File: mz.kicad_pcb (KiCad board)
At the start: 2 copper layers, 79 x 68 mm, 32 parts, among them CON1 USB-MINI-B, P1 JTAG, P2 CONN_20, P3 CONN_20, P4 CONN_20, P5 CONN_20, P6 CONN_20, P7 CONN_20, SW1 RESET, U1 NCP1117ST50T3G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

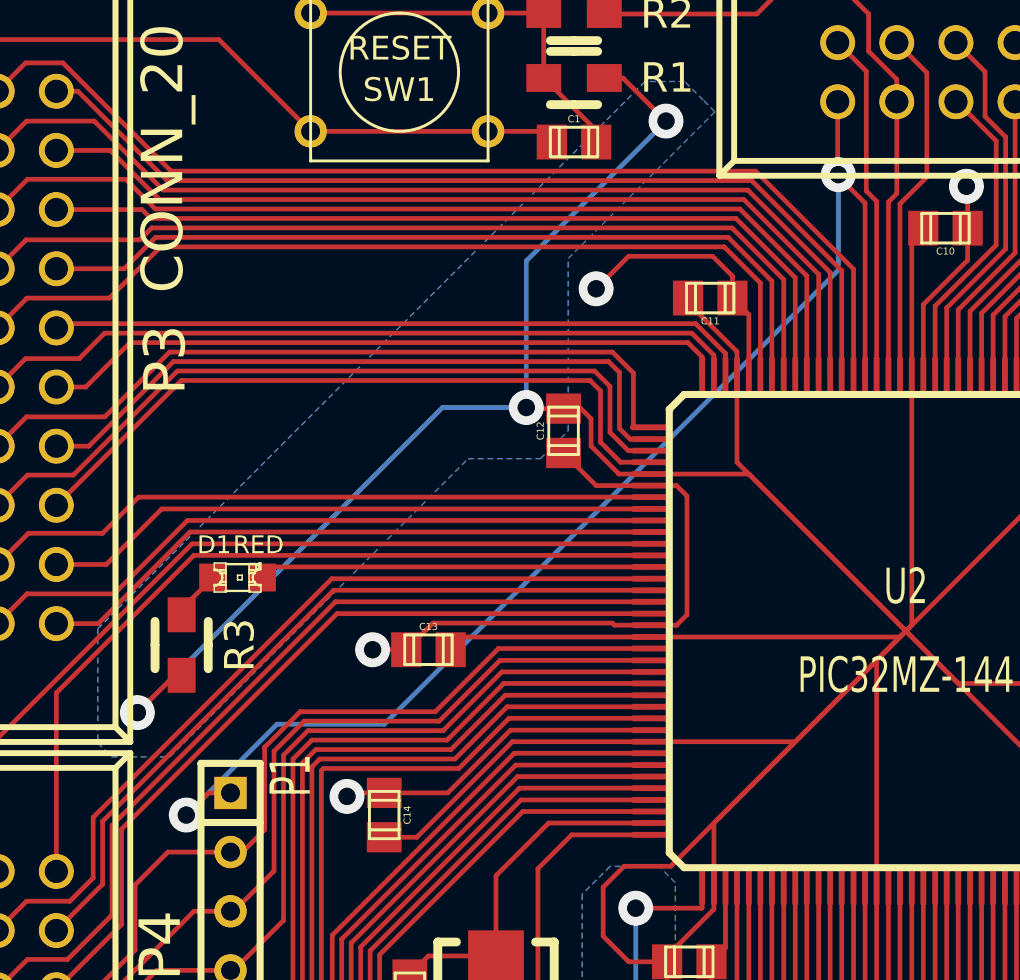
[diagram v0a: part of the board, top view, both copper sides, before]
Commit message: PDF schematics on docs/
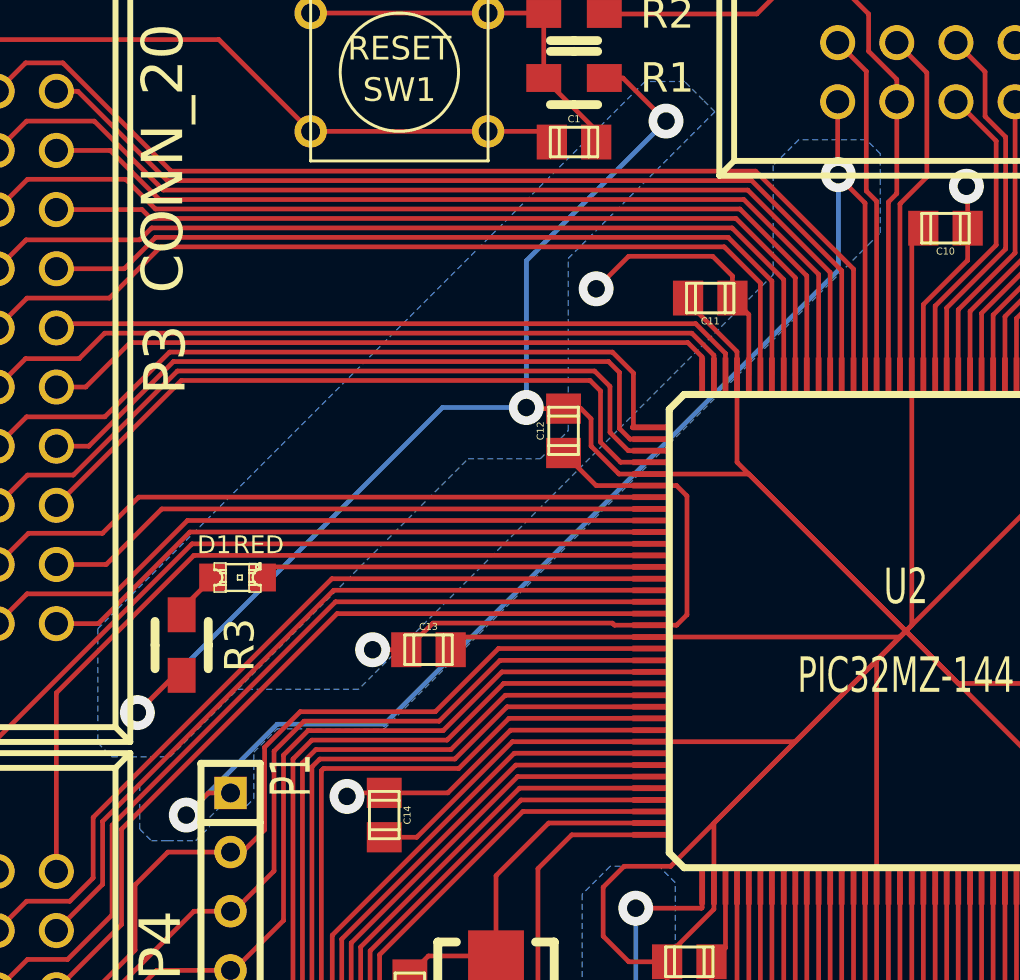
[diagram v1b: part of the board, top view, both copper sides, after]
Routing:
- added copper zone on B.Cu, net /JTAG_TMS
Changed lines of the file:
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@@
+    )
+  )
+  (zone (net 12) (net_name /JTAG_TMS) (layer B.Cu) (hatch edge 0.508)
+    (priority 2)
+    (connect_pads yes (clearance 0.381))
+    (min_thickness 0.254)
+    (fill yes (arc_segments 16) (thermal_gap 1.1938) (thermal_bridge_width 0.508))
+    (polygon
+      (pts
+        (xy 116.8 114) (xy 118 114) (xy 118.6 113.4) (xy 118.6 113) (xy 119.1 112.5)
+        (xy 120.2 112.5) (xy 120.5 112.2) (xy 120.5 110.2) (xy 121.5 109.2) (xy 126.1 109.2)
+        (xy 146.9 88.4) (xy 147.4 87.9) (xy 147.4 84.5) (xy 146.8 83.9) (xy 143.9 83.9)
+        (xy 142.8 85) (xy 142.8 89.7) (xy 125 107.5) (xy 119.7 107.5) (xy 116.2 111)
+        (xy 115.6 111.6) (xy 115.6 113.5) (xy 116.1 114) (xy 116.7 114)
+      )
     )
   )

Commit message: Add power led
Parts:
- added D2: RED, LEDs:LED-0805, F.Cu at (126.7, 129.3)
- added R4: 220R, Resistors_SMD:Resistor_SMD0805_HandSoldering, F.Cu at (123.6, 131.3)
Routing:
- net +3.3V: track 310.0 -> 314.6 mm
- net Net-(D2-Pad1): track 0.00 -> 2.34 mm
- net GND: track 266.6 -> 268.6 mm
